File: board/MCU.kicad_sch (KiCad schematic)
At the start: 26 parts, among them SW1 SW_Push, U1 STSPIN32G4TR

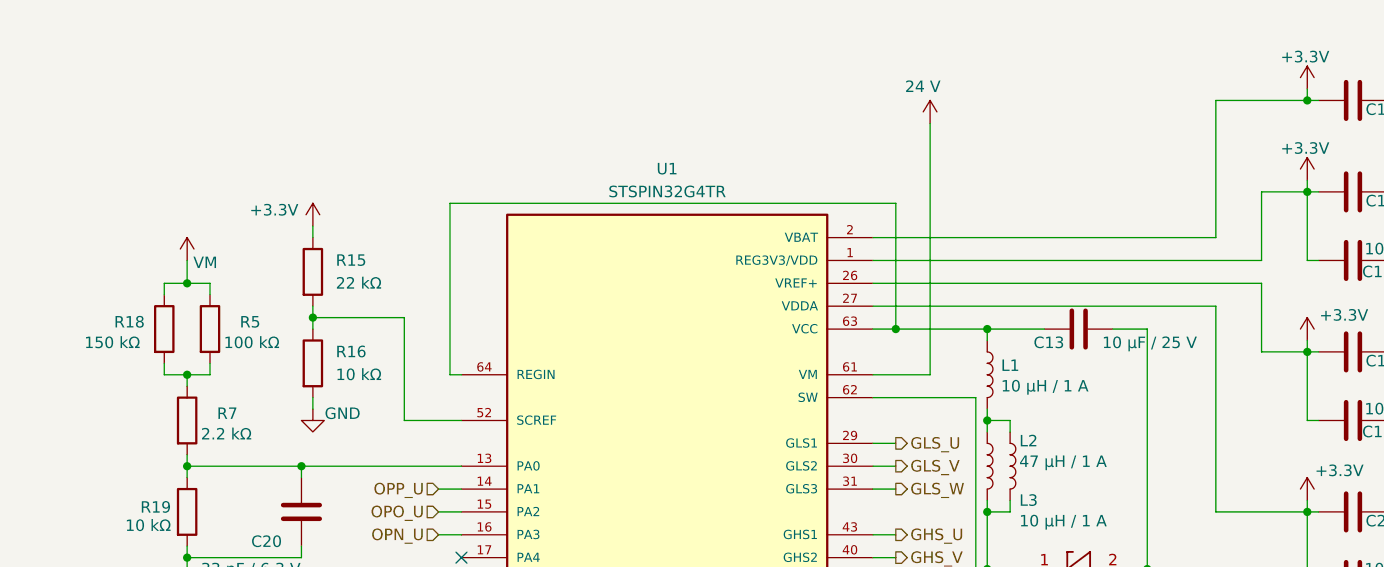
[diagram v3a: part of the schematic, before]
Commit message: Regrouped components on the layout into a rough draft before the next set of zoning and tracing.
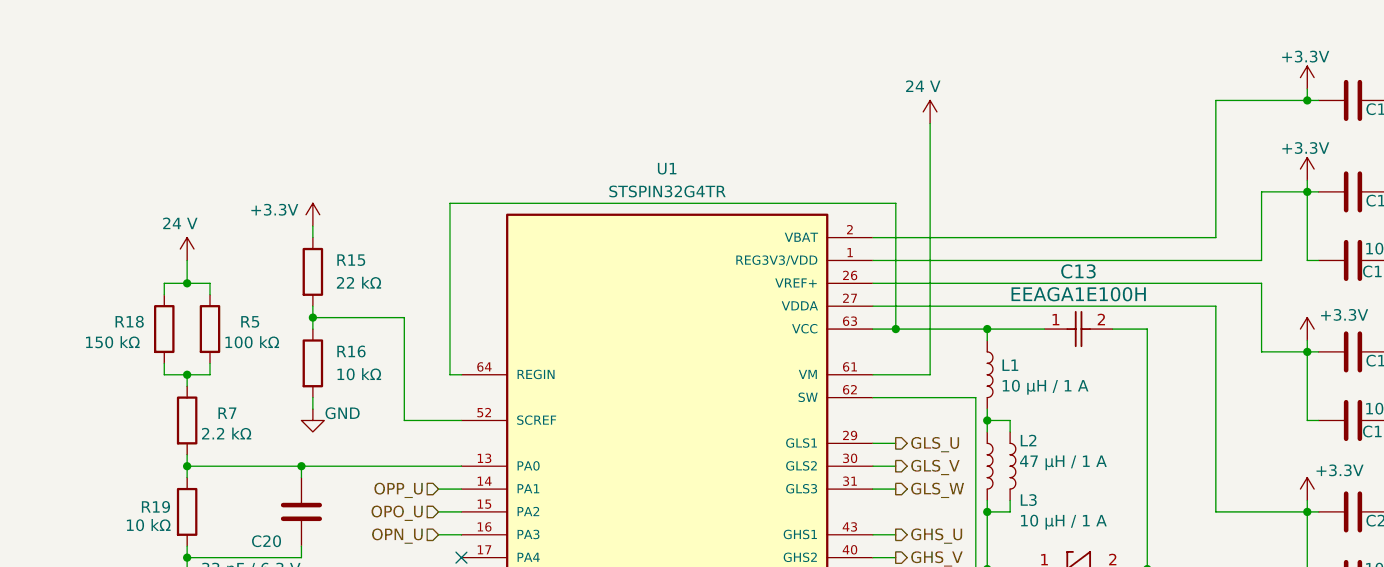
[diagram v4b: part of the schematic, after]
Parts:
- removed C13: 10 μF / 25 V, BrushlessMocoBoard:CAPPRD250W45D400H700, symbol Device:C
- added C13: EEAGA1E100H, CAP_PAN_4X7_PAN, symbol 25V Cap:EEAGA1E100H
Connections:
- net VM is gone; now on net 24 V: R18.1, R5.1
- net GND: now also C13.2
- net at L1.1, U1.63 (VCC), U1.64 (REGIN): now also C13.1
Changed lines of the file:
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@@
-	)
-	(symbol
-		(lib_id "Device:C")
-		(at 167.64 73.66 90)
-		(unit 1)
-		(exclude_from_sim no)
-		(in_bom yes)
-		(on_board yes)
-		(dnp no)
-		(property "Reference" "C13"
-			(at 164.338 75.184 90)
-			(effects
-				(font
-					(size 1.27 1.27)
-				)
-			)
-		)
-		(property "Value" "10 μF / 25 V"
-			(at 175.514 75.184 90)
-			(effects
-				(font
-					(size 1.27 1.27)
-				)
-			)
-		)
-		(property "Footprint" "BrushlessMocoBoard:CAPPRD250W45D400H700"
-			(at 171.45 72.6948 0)
-			(effects
-				(font
-					(size 1.27 1.27)
-				)
-				(hide yes)
-			)
-		)
-		(property "Datasheet" "~"
-			(at 167.64 73.66 0)
-			(effects
-				(font
-					(size 1.27 1.27)
-				)
-				(hide yes)
-			)
-		)
-		(property "Description" "Unpolarized capacitor"
-			(at 167.64 73.66 0)
-			(effects
-				(font
-					(size 1.27 1.27)
-				)
-				(hide yes)
-			)
-		)
-		(pin "1"
-		)
-		(pin "2"
-		)
-		(instances
-			(project "BrushlessMocoBoard"
-				(path "/1ef8bc88-f0df-4a97-862b-c4b9ec3b4ed0/02edeb2f-867a-4e66-ac0c-df2434256428"
-					(reference "C13")
-					(unit 1)
-				)
-			)
-		)
 	)
 	(symbol
@@
 				(path "/1ef8bc88-f0df-4a97-862b-c4b9ec3b4ed0/02edeb2f-867a-4e66-ac0c-df2434256428"
 					(reference "#PWR046")
-					(unit 1)
-				)
-			)
-		)
-	)
-	(symbol
-		(lib_id "power:VCC")
-		(at 68.58 66.04 0)
-		(unit 1)
-		(exclude_from_sim no)
-		(in_bom yes)
-		(on_board yes)
-		(dnp no)
-		(property "Reference" "#PWR037"
-			(at 68.58 69.85 0)
-			(effects
-				(font
-					(size 1.27 1.27)
-				)
-				(hide yes)
-			)
-		)
-		(property "Value" "VM"
-			(at 70.612 66.2941 0)
-			(effects
-				(font
-					(size 1.27 1.27)
-				)
-			)
-		)
-		(property "Footprint" ""
-			(at 68.58 66.04 0)
-			(effects
-				(font
-					(size 1.27 1.27)
-				)
-				(hide yes)
-			)
-		)
-		(property "Datasheet" ""
-			(at 68.58 66.04 0)
-			(effects
-				(font
-					(size 1.27 1.27)
-				)
-				(hide yes)
-			)
-		)
-		(property "Description" "Power symbol creates a global label with name \"VCC\""
-			(at 68.58 66.04 0)
-			(effects
-				(font
-					(size 1.27 1.27)
-				)
-				(hide yes)
-			)
-		)
-		(pin "1"
-		)
-		(instances
-			(project "BrushlessMocoBoard"
-				(path "/1ef8bc88-f0df-4a97-862b-c4b9ec3b4ed0/02edeb2f-867a-4e66-ac0c-df2434256428"
-					(reference "#PWR037")
 					(unit 1)
 				)
@@
 	)
 	(symbol
+		(lib_id "power:VCC")
+		(at 68.58 66.04 0)
+		(unit 1)
+		(exclude_from_sim no)
+		(in_bom yes)
+		(on_board yes)
+		(dnp no)
+		(property "Reference" "#PWR037"
+			(at 68.58 69.85 0)
+			(effects
+				(font
+					(size 1.27 1.27)
+				)
+				(hide yes)
+			)
+		)
+		(property "Value" "24 V"
+			(at 65.786 61.976 0)
+			(effects
+				(font
+					(size 1.27 1.27)
+				)
+				(justify left)
+			)
+		)
+		(property "Footprint" ""
+			(at 68.58 66.04 0)
+			(effects
+				(font
+					(size 1.27 1.27)
+				)
+				(hide yes)
+			)
+		)
+		(property "Datasheet" ""
+			(at 68.58 66.04 0)
+			(effects
+				(font
+					(size 1.27 1.27)
+				)
+				(hide yes)
+			)
+		)
+		(property "Description" "Power symbol creates a global label with name \"VCC\""
+			(at 68.58 66.04 0)
+			(effects
+				(font
+					(size 1.27 1.27)
+				)
+				(hide yes)
+			)
+		)
+		(pin "1"
+		)
+		(instances
+			(project "BrushlessMocoBoard"
+				(path "/1ef8bc88-f0df-4a97-862b-c4b9ec3b4ed0/02edeb2f-867a-4e66-ac0c-df2434256428"
+					(reference "#PWR037")
+					(unit 1)
+				)
+			)
+		)
+	)
+	(symbol
 		(lib_id "Device:C")
 		(at 81.28 167.64 0)
@@
 					(unit 1)
 				)
+			)
+		)
+	)
+	(symbol
+		(lib_id "25V Cap:EEAGA1E100H")
+		(at 163.83 73.66 0)
+		(unit 1)
+		(exclude_from_sim no)
+		(in_bom yes)
+		(on_board yes)
+		(dnp no)
+		(fields_autoplaced yes)
+		(property "Reference" "C13"
+			(at 167.64 67.31 0)
+			(effects
+				(font
+					(size 1.524 1.524)
+				)
+			)
+		)
+		(property "Value" "EEAGA1E100H"
+			(at 167.64 69.85 0)
+			(effects
+				(font
+					(size 1.524 1.524)
+				)
+			)
+		)
+		(property "Footprint" "CAP_PAN_4X7_PAN"
+			(at 163.83 73.66 0)
+			(effects
+				(font
+					(size 1.27 1.27)
+					(italic yes)
+				)
+				(hide yes)
+			)
+		)
+		(property "Datasheet" "EEAGA1E100H"
+			(at 163.83 73.66 0)
+			(effects
+				(font
+					(size 1.27 1.27)
+					(italic yes)
+				)
+				(hide yes)
+			)
+		)
+		(property "Description" ""
+			(at 163.83 73.66 0)
+			(effects
+				(font
+					(size 1.27 1.27)
+				)
+				(hide yes)
+			)
+		)
+		(pin "2"
+		)
+		(pin "1"
+		)
+		(instances
+			(project ""
+				(path "/1ef8bc88-f0df-4a97-862b-c4b9ec3b4ed0/02edeb2f-867a-4e66-ac0c-df2434256428"
+					(reference "C13")
+					(unit 1)
+				)

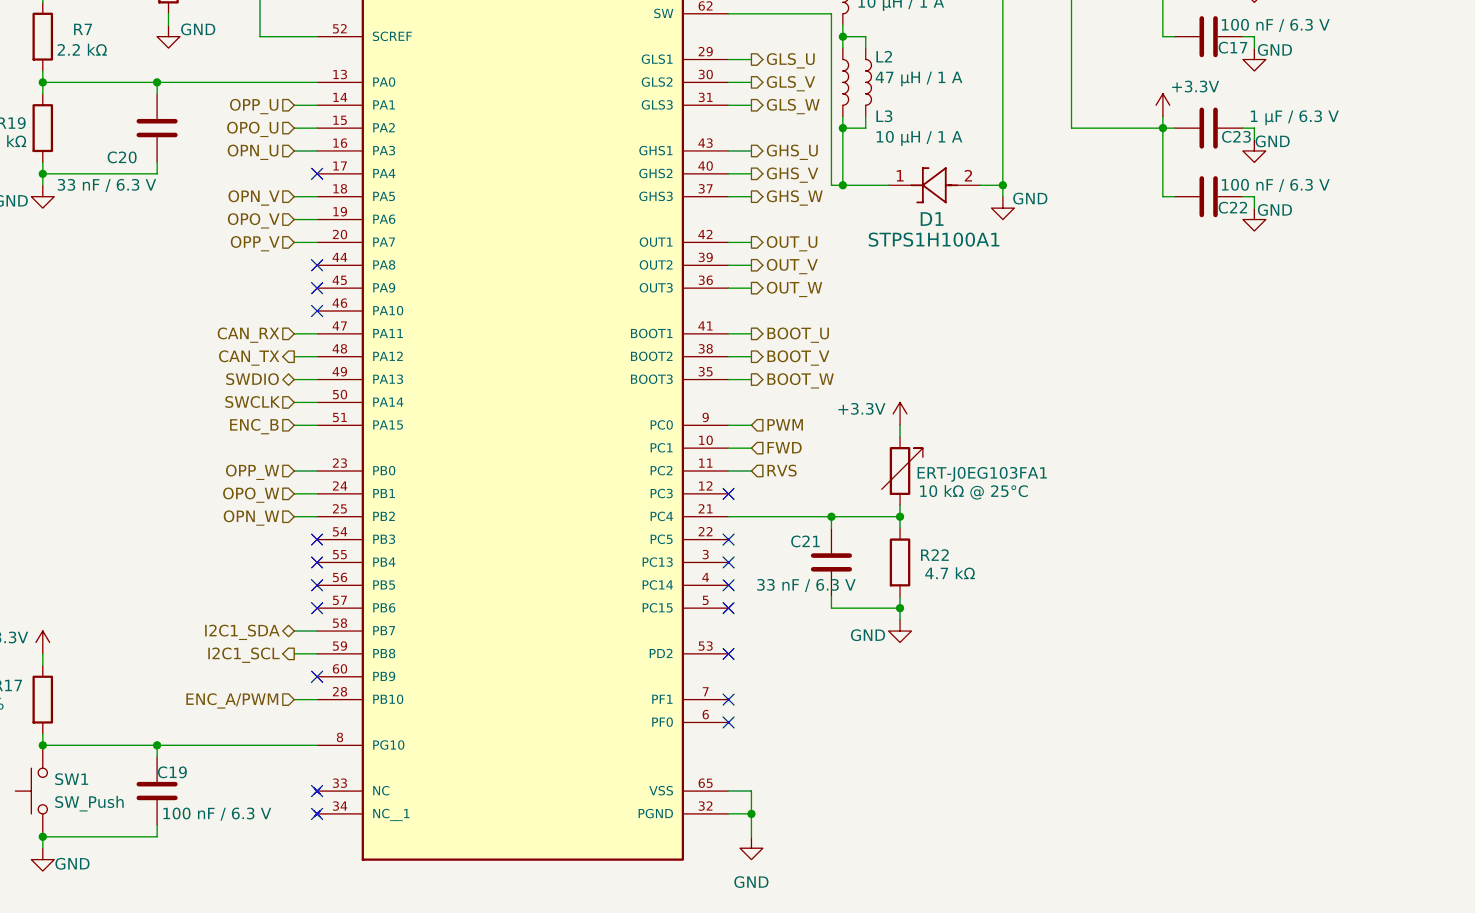
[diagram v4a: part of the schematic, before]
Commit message: Significant progress on board layout. Added GPIO and UART pins, also rearranged encoder and I2C MCU pins.
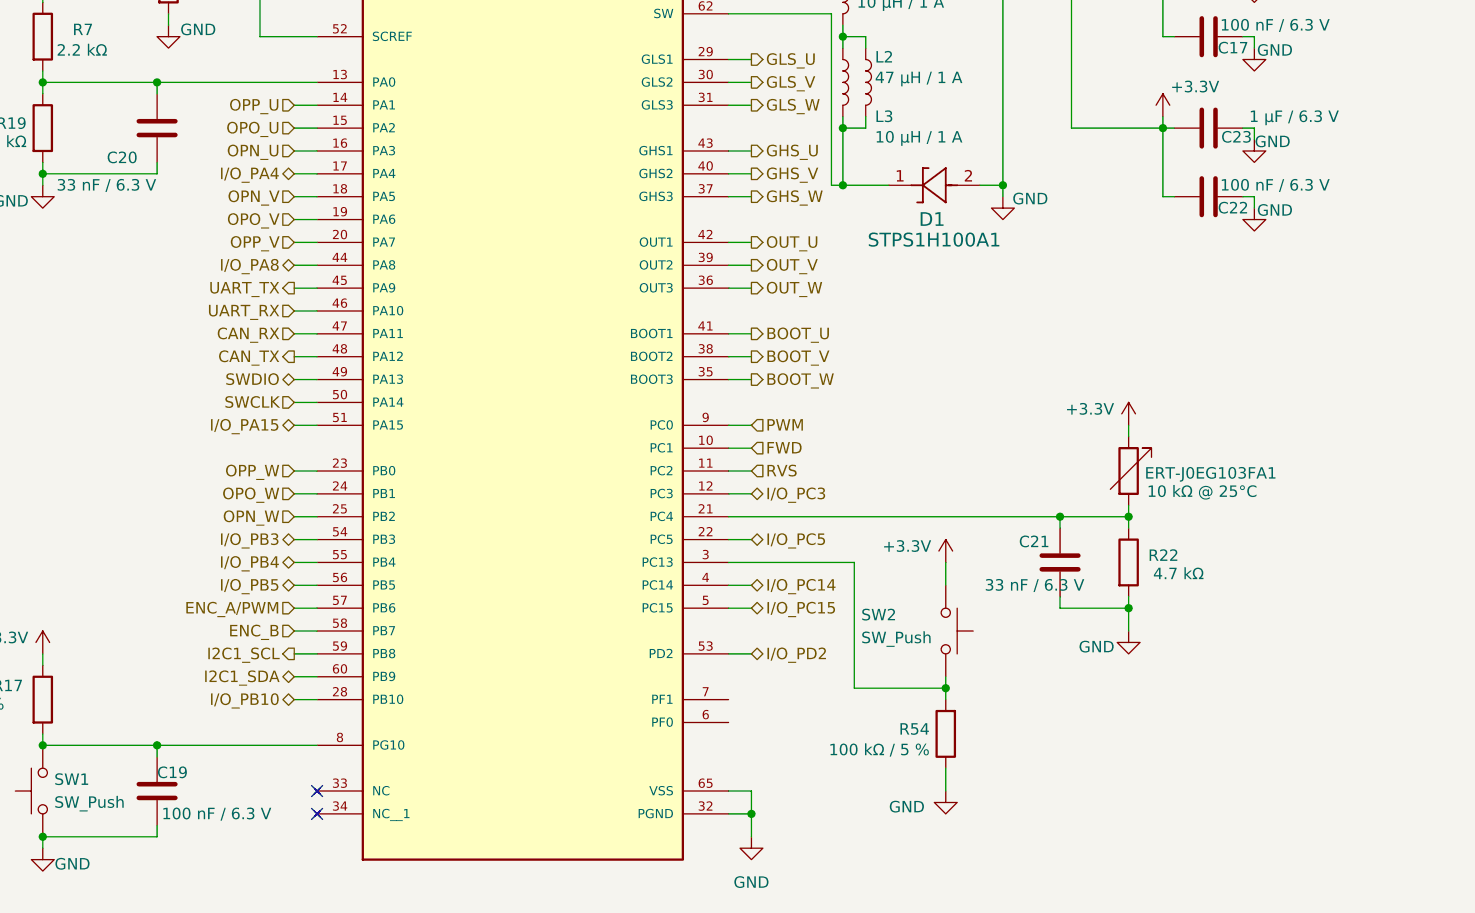
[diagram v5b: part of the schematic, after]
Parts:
- added R54: 100 kΩ / 5 %, Resistor_SMD:R_0603_1608Metric_Pad0.98x0.95mm_HandSolder, symbol Device:R
- added SW2: SW_Push, MRDT_Switches:SW_SPST_TL3305A, symbol Switch:SW_Push
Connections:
- net +3.3V: now also SW2.1
- net ENC_A/PWM: now also U1.57 (PB6); no longer U1.28 (PB10)
- net ENC_B: now also U1.58 (PB7); no longer U1.51 (PA15)
- net GND: now also R54.1
- net I2C1_SDA: now also U1.60 (PB9); no longer U1.58 (PB7)
- net I/O_PC3: now reaches U1.12 (PC3)
- net I/O_PA4: now reaches U1.17 (PA4)
- net I/O_PC5: now reaches U1.22 (PC5)
- net at U1.3 (PC13): now also R54.2, SW2.2
- net I/O_PC14: now reaches U1.4 (PC14)
- net I/O_PA8: now reaches U1.44 (PA8)
- net UART_TX: now reaches U1.45 (PA9)
- net UART_RX: now reaches U1.46 (PA10)
- net I/O_PC15: now reaches U1.5 (PC15)
- net I/O_PD2: now reaches U1.53 (PD2)
- net I/O_PB3: now reaches U1.54 (PB3)
- net I/O_PB4: now reaches U1.55 (PB4)
- net I/O_PB5: now reaches U1.56 (PB5)
- new net I/O_PA15: U1.51 (PA15)
- new net I/O_PB10: U1.28 (PB10)
- no-connect marks 19 -> 2
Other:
- moved on the sheet: C21, ERT-J0EG103FA1, R22

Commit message: Updated footprints to fix issues found in board review.
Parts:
- C13: footprint CAP_PAN_4X7_PAN -> BrushlessMocoBoard:CAP_PAN_4X7_PAN
- C20, C21: footprint Capacitor_SMD:C_0201_0603Metric_Pad0.64x0.40mm_HandSolder -> Capacitor_SMD:C_0603_1608Metric_Pad1.08x0.95mm_HandSolder
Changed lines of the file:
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@@
 			)
 		)
-		(property "Footprint" "Capacitor_SMD:C_0201_0603Metric_Pad0.64x0.40mm_HandSolder"
+		(property "Footprint" "Capacitor_SMD:C_0603_1608Metric_Pad1.08x0.95mm_HandSolder"
 			(at 82.2452 97.79 0)
 			(effects
@@
 			)
 		)
-		(property "Footprint" "CAP_PAN_4X7_PAN"
+		(property "Footprint" "BrushlessMocoBoard:CAP_PAN_4X7_PAN"
 			(at 163.83 73.66 0)
 			(effects
@@
 			)
 		)
-		(property "Footprint" "Capacitor_SMD:C_0201_0603Metric_Pad0.64x0.40mm_HandSolder"
+		(property "Footprint" "Capacitor_SMD:C_0603_1608Metric_Pad1.08x0.95mm_HandSolder"
 			(at 182.5752 146.05 0)
 			(effects

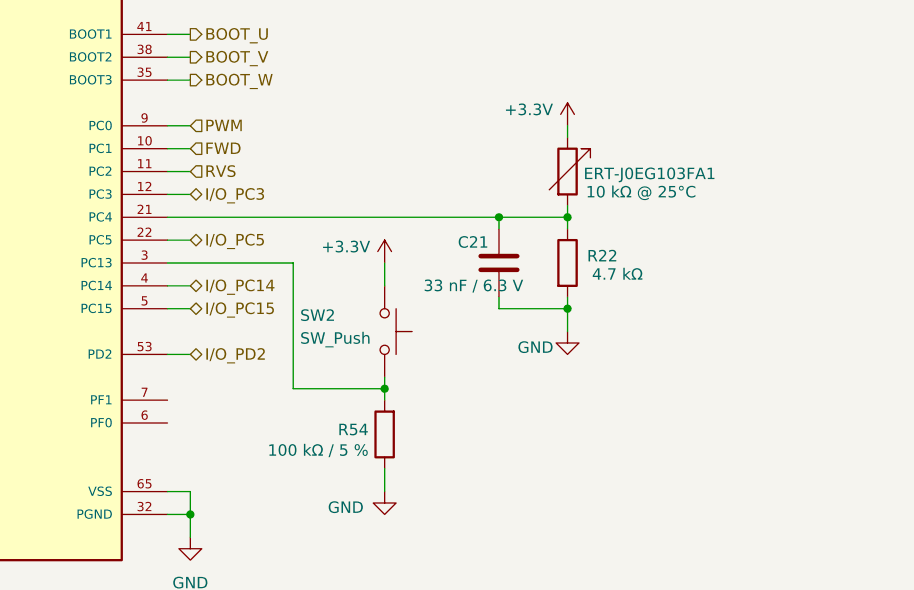
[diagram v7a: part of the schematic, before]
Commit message: First draft of wiring for the layout finished.
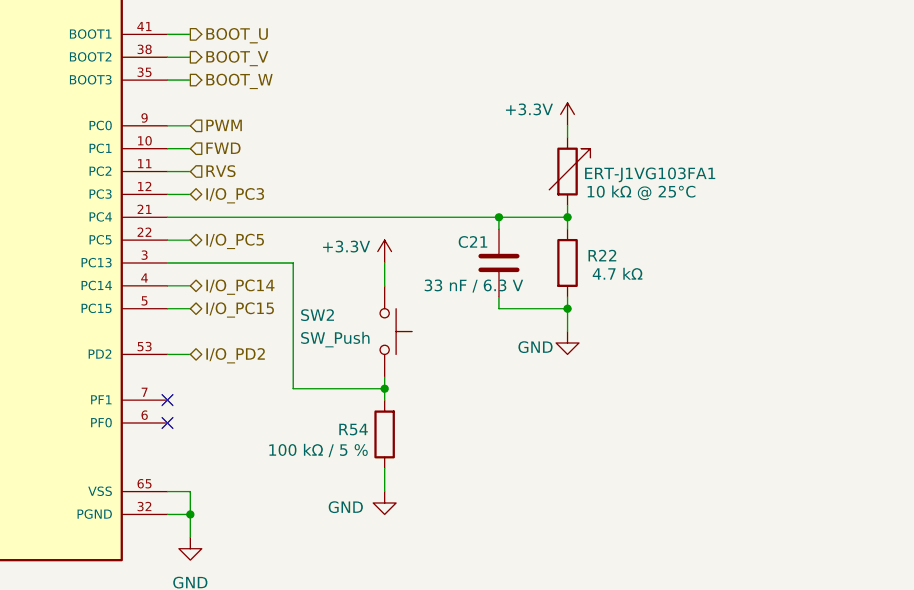
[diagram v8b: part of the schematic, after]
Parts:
- ERT-J1VG103FA1: renamed from ERT-J0EG103FA1; footprint Resistor_SMD:R_0402_1005Metric_Pad0.72x0.64mm_HandSolder -> Resistor_SMD:R_0603_1608Metric_Pad0.98x0.95mm_HandSolder
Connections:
- no-connect marks 2 -> 4
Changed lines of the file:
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@@
 	)
 	(no_connect
+		(at 144.78 157.48)
+	)
+	(no_connect
 		(at 99.06 167.64)
 	)
@@
 		(at 99.06 170.18)
 	)
+	(no_connect
+		(at 144.78 160.02)
+	)
 	(wire
 		(pts
@@
 		(on_board yes)
 		(dnp no)
-		(property "Reference" "ERT-J0EG103FA1"
+		(property "Reference" "ERT-J1VG103FA1"
 			(at 191.008 132.334 0)
 			(effects
@@
 			)
 		)
-		(property "Footprint" "Resistor_SMD:R_0402_1005Metric_Pad0.72x0.64mm_HandSolder"
+		(property "Footprint" "Resistor_SMD:R_0603_1608Metric_Pad0.98x0.95mm_HandSolder"
 			(at 187.452 132.08 90)
 			(effects
@@
 			(project "BrushlessMocoBoard"
 				(path "/1ef8bc88-f0df-4a97-862b-c4b9ec3b4ed0/02edeb2f-867a-4e66-ac0c-df2434256428"
-					(reference "ERT-J0EG103FA1")
+					(reference "ERT-J1VG103FA1")
 					(unit 1)
 				)
